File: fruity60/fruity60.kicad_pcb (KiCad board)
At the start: 2 copper layers, 126 parts

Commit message: Basic layout of switches
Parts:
- MX4A1: footprint MX_Only:MXOnly-1U -> MX_Only:MXOnly-1.5U
- moved MX0 382.1 mm to (-69.8, 65.1)
- moved D24 375.6 mm to (-26.4, 2.21)
- moved D3 375.6 mm to (-46.6, 26.4)
- moved D5 375.6 mm to (-20.6, 2.21)
- moved D11 375.6 mm to (-40.8, 19.7)
- moved D13 375.6 mm to (-46.6, 23.1)
- moved D27 375.6 mm to (-46.6, 19.7)
- moved D6 375.6 mm to (-26.4, 5.56)
- moved MX1 348.0 mm to (-50.8, 65.1)
- moved MX3 344.7 mm to (-12.7, 65.1)
- moved MX2 330.1 mm to (-31.8, 65.1)
- moved MX11 309.5 mm to (-41.3, 84.1)
- moved MX12 307.5 mm to (-22.2, 84.1)
- moved D19 303.2 mm to (154.6, 0.21)
- moved D32 303.2 mm to (148.9, 0.21)
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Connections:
- JP1 pad 1: /DFU -> (no net)
- JP1 pad 13: GND -> (no net)
- JP1 pad 14: /AREF -> (no net)
- JP1 pad 15: +3V3 -> (no net)
- JP1 pad 16: /RST -> (no net)
- JP1 pad 4: /MISO -> (no net)
- JP1 pad 5: /MOSI -> (no net)
- JP1 pad 6: /SCK -> (no net)
- JP2 pad 1: VBAT -> (no net)
- JP2 pad 2: /EN -> (no net)
- JP2 pad 3: VBUS -> (no net)

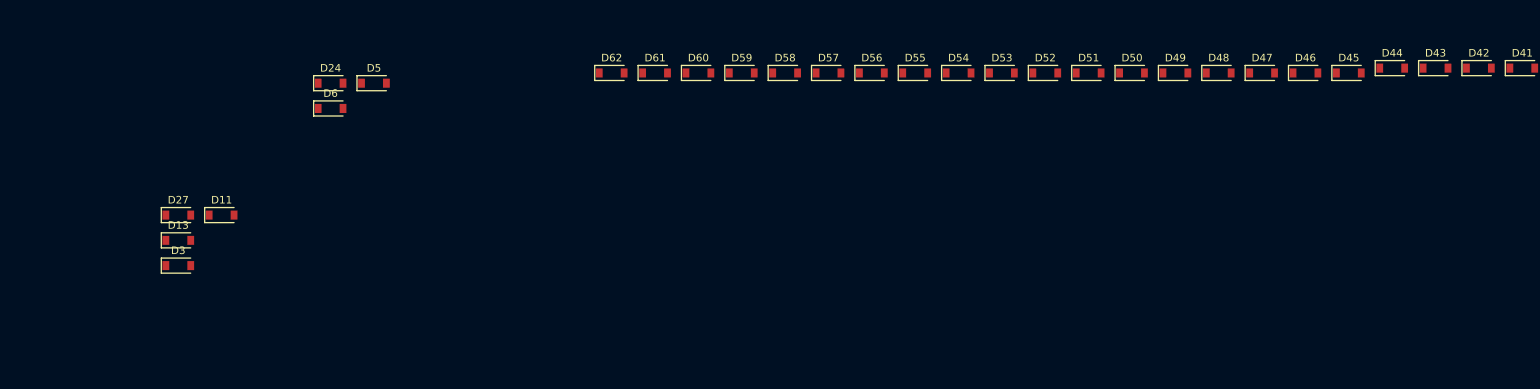
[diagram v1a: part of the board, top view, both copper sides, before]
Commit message: move some diodes around
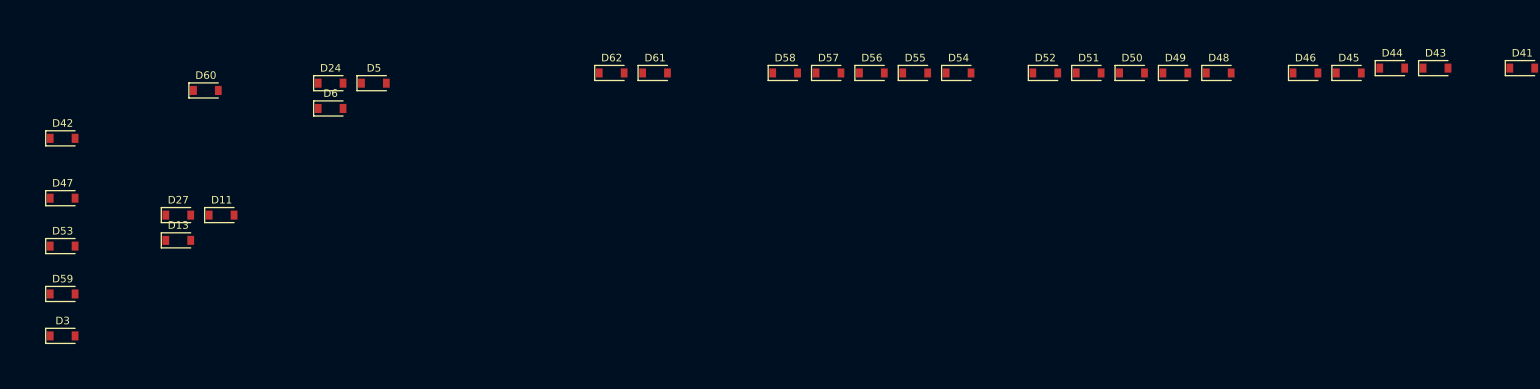
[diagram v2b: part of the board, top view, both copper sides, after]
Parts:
- moved D42 188.0 mm to (-61.9, 9.53)
- moved D47 159.9 mm to (-61.9, 17.5)
- moved D53 126.7 mm to (-61.9, 23.8)
- moved D59 94.7 mm to (-61.9, 30.2)
- moved D60 65.4 mm to (-42.9, 3.17)
- moved D3 17.9 mm to (-61.9, 35.7)
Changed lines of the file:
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@@
     (uvia_dia 0.3)
     (uvia_drill 0.1)
-    (add_net +3V3)
-    (add_net /AREF)
-    (add_net /DFU)
-    (add_net /EN)
-    (add_net /MISO)
-    (add_net /MOSI)
-    (add_net /RST)
-    (add_net /SCK)
     (add_net B5)
     (add_net B6)
@@
     (add_net F6)
     (add_net F7)
-    (add_net GND)
     (add_net "Net-(D1-Pad2)")
     (add_net "Net-(D10-Pad2)")
@@
     (add_net "Net-(D8-Pad2)")
     (add_net "Net-(D9-Pad2)")
-    (add_net VBAT)
-    (add_net VBUS)
   )
   (module MX_Only:MXOnly-1.5U (layer F.Cu)
@@
   )
   (module Diodes_SMD:D_SOD-123 (layer F.Cu)
-    (at 22.3925 0.855)
+    (at -42.925 3.175)
     (descr SOD-123)
     (tags SOD-123)
@@
   )
   (module Diodes_SMD:D_SOD-123 (layer F.Cu)
-    (at 28.1425 0.855)
+    (at -61.9125 30.1625)
     (descr SOD-123)
     (tags SOD-123)
@@
   )
   (module Diodes_SMD:D_SOD-123 (layer F.Cu)
-    (at 62.6425 0.855)
+    (at -61.9125 23.8125)
     (descr SOD-123)
     (tags SOD-123)
@@
   )
   (module Diodes_SMD:D_SOD-123 (layer F.Cu)
-    (at 97.1425 0.855)
+    (at -61.9125 17.4625)
     (descr SOD-123)
     (tags SOD-123)
@@
   )
   (module Diodes_SMD:D_SOD-123 (layer F.Cu)
-    (at 125.8925 0.215)
+    (at -61.9125 9.525)
     (descr SOD-123)
     (tags SOD-123)
@@
   )
   (module Diodes_SMD:D_SOD-123 (layer F.Cu)
-    (at -46.5825 26.4025)
+    (at -61.9125 35.71875)
     (descr SOD-123)
     (tags SOD-123)

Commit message: flip diodes. Thanks Skully
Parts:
- removed the D1 at (193.7, 23.8)
- removed the D27 at (-46.6, 19.7)
- added D0: D_Small, Diodes_SMD:D_SOD-123, B.Cu at (-70.6, 49.2)
- added D34: D_Small, Diodes_SMD:D_SOD-123, B.Cu at (10.3, 40.5)
- D1: renamed from D7; moved to B.Cu
- D10: renamed from D2; moved to B.Cu
- D11: renamed from D8; moved to B.Cu
- D12: renamed from D14; moved to B.Cu
- D13: renamed from D20; moved to B.Cu
- D14: renamed from D25; moved to B.Cu
- D15: renamed from D30; moved to B.Cu
- D16: renamed from D36; moved to B.Cu
- D17: renamed from D41; moved to B.Cu
- D18: renamed from D46; moved to B.Cu
- D19: renamed from D52; moved to B.Cu
- D1A1: renamed from D58; moved to B.Cu
- D2: renamed from D13; moved to B.Cu
- D20: renamed from D3; moved to B.Cu
- D21: renamed from D9; moved to B.Cu
- D22: renamed from D15; moved to B.Cu
- D23: renamed from D21; moved to B.Cu
- D24: renamed from D26; moved to B.Cu
- D25: renamed from D31; moved to B.Cu
- D26: renamed from D37; moved to B.Cu
- D27: renamed from D42; moved to B.Cu
- D28: renamed from D47; moved to B.Cu
- D29: renamed from D53; moved to B.Cu
- D2A1: renamed from D59; moved to B.Cu
- D3: renamed from D19; moved to B.Cu
- D30: renamed from D4; moved to B.Cu
- D31: renamed from D10; moved to B.Cu
- D32: renamed from D16; moved to B.Cu
- D33: renamed from D22; moved to B.Cu
- D35: renamed from D32; moved to B.Cu
- D36: renamed from D38; moved to B.Cu
- D37: renamed from D43; moved to B.Cu
- D38: renamed from D48; moved to B.Cu
- D39: renamed from D54; moved to B.Cu
- D3A1: renamed from D60; moved to B.Cu
- D4: renamed from D24; moved to B.Cu
- D40: renamed from D5; moved to B.Cu
- D41: renamed from D11; moved to B.Cu
- D42: renamed from D17; moved to B.Cu
- D45: renamed from D33; moved to B.Cu
- D48: renamed from D49; moved to B.Cu
- D49: renamed from D55; moved to B.Cu
- D4A1: renamed from D61; moved to B.Cu
- D5: renamed from D29; moved to B.Cu
- D50: renamed from D6; moved to B.Cu
- D51: renamed from D12; moved to B.Cu
- D52: renamed from D18; moved to B.Cu
- D53: renamed from D23; moved to B.Cu
- D54: renamed from D28; moved to B.Cu
- D55: renamed from D34; moved to B.Cu
- D56: renamed from D39; moved to B.Cu
- D57: renamed from D44; moved to B.Cu
- D58: renamed from D50; moved to B.Cu
- D59: renamed from D56; moved to B.Cu
- D5A1: renamed from D62; moved to B.Cu
- D6: renamed from D35; moved to B.Cu
- D7: renamed from D40; moved to B.Cu
- D8: renamed from D45; moved to B.Cu
- D9: renamed from D51; moved to B.Cu
- DA1: renamed from D57; moved to B.Cu
- moved D10 269.3 mm to (-68.3, 46.8), turned to 270 degrees
- moved D1 260.6 mm to (-52.4, 50.0), turned to 270 degrees
- moved D30 250.6 mm to (-63.5, 42.9), turned to 270 degrees
- moved D21 236.2 mm to (-47.6, 45.2), turned to 90 degrees
- moved D12 235.2 mm to (-33.3, 47.6), turned to 270 degrees
- moved D11 234.8 mm to (-50.0, 47.6), turned to 270 degrees
- moved D51 227.7 mm to (-40.5, 38.1), turned to 270 degrees
- moved D22 226.0 mm to (-31.0, 45.2), turned to 270 degrees
- moved D31 219.7 mm to (-45.2, 42.9), turned to 270 degrees
- moved D32 210.0 mm to (-28.6, 42.9), turned to 270 degrees
- moved D33 203.8 mm to (-8.73, 40.5), turned to 270 degrees
- moved D23 199.9 mm to (-11.1, 42.9), turned to 270 degrees
- moved D14 197.0 mm to (5.56, 45.2), turned to 270 degrees
- moved D52 192.0 mm to (-23.8, 38.1), turned to 270 degrees
- moved D42 190.3 mm to (-26.2, 40.5), turned to 270 degrees
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
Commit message: Align diodes better
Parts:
- moved D18 8.77 mm to (87.3, 48.4)
- moved D38 8.77 mm to (92.1, 43.7)
- moved D48 8.77 mm to (94.5, 41.3)
- moved D58 8.77 mm to (96.8, 38.9)
- moved D8 8.77 mm to (84.9, 50.8)
- moved D28 8.77 mm to (89.7, 46.0)
- moved D17 7.98 mm to (68.3, 46.0)
- moved D27 7.98 mm to (70.6, 43.7)
- moved D37 7.98 mm to (73.0, 41.3)
- moved D57 7.98 mm to (75.4, 38.9)
- moved D7 7.98 mm to (65.9, 48.4)
- moved D3A1 7.19 mm to (130.2, 43.7)
- moved D4A1 7.19 mm to (132.6, 41.3)
- moved D25 7.19 mm to (32.5, 46.0)
- moved D36 7.19 mm to (54.0, 41.3)
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
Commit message: Line up diodes for more pleasing look
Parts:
- D0, D1, D10, D11, D12, D13, D14, D15, D16, D17, D18, D19, D1A1, D2, D20, D21, D22, D23, D24, D25, D26, D27, D28, D29, D2A1, D3, D30, D31, D32, D33, D34, D35, D36, D37, D38, D39, D3A1, D4, D40, D41, D42, D45, D48, D49, D4A1, D5, D50, D51, D52, D53, D54, D55, D56, D57, D58, D59, D5A1, D6, D7, D8, D9, DA1: moved to F.Cu
- moved D50 198.0 mm to (142.1, 50.8)
- moved D51 181.4 mm to (144.5, 50.8)
- moved D52 164.7 mm to (146.8, 50.8)
- moved D53 150.5 mm to (149.2, 50.8)
- moved D54 133.9 mm to (151.6, 50.8)
- moved D55 114.9 mm to (154.0, 50.8)
- moved D56 99.9 mm to (155.6, 50.8)
- moved D57 83.4 mm to (158.0, 50.8)
- moved D58 64.6 mm to (160.3, 50.8)
- moved D59 48.3 mm to (162.7, 50.8)
- moved D5A1 32.4 mm to (165.1, 50.8)
- moved D13 2.38 mm to (-7.94, 48.4)
- moved D14 2.38 mm to (11.1, 48.4)
- moved D16 2.38 mm to (49.2, 48.4)
- moved D17 2.38 mm to (68.3, 48.4)
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
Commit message: Clean ups
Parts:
- moved D56 1.12 mm to (156.4, 50.0)
- moved D5A1 1.12 mm to (165.9, 50.0)
- moved D57 1.12 mm to (158.8, 50.0)
- moved D58 1.12 mm to (161.1, 50.0)
- moved D59 1.12 mm to (163.5, 50.0)
- moved D50 0.79 mm to (142.1, 50.0)
- moved D51 0.79 mm to (144.5, 50.0)
- moved D52 0.79 mm to (146.8, 50.0)
- moved D53 0.79 mm to (149.2, 50.0)
- moved D54 0.79 mm to (151.6, 50.0)
- moved D55 0.79 mm to (154.0, 50.0)

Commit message: Use 2.54 straight headers not angled
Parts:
- JP1: footprint Pin_Headers:Pin_Header_Angled_1x16_Pitch1.00mm -> Pin_Headers:Pin_Header_Straight_1x16_Pitch2.54mm
- JP2: footprint Pin_Headers:Pin_Header_Angled_1x12_Pitch1.00mm -> Pin_Headers:Pin_Header_Straight_1x12_Pitch2.54mm
- moved JP1 31.6 mm to (165.9, 39.7), turned to 90 degrees
- moved JP2 13.7 mm to (193.7, 50.8), turned to 270 degrees
- moved D50 7.98 mm to (134.1, 50.8)
- moved D51 7.98 mm to (136.5, 50.8)
- moved D52 7.98 mm to (138.9, 50.8)
- moved D53 7.98 mm to (141.3, 50.8)
- moved D54 7.98 mm to (143.7, 50.8)
- moved D55 7.98 mm to (146.1, 50.8)
- moved D56 7.98 mm to (148.4, 50.8)
- moved D57 7.98 mm to (150.8, 50.8)
- moved D58 7.98 mm to (153.2, 50.8)
- moved D59 7.98 mm to (155.6, 50.8)
- moved D5A1 7.98 mm to (158.0, 50.8)

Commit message: Routing weirdness
 May need to change footprint for diodes
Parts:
- moved D40 11.1 mm to (-57.9, 52.4)
- moved D41 11.1 mm to (-38.9, 52.4)
- moved D42 11.1 mm to (-19.8, 52.4)
- moved D48 11.1 mm to (94.5, 52.4)
- moved D49 11.1 mm to (113.5, 52.4)
- moved D4A1 11.1 mm to (132.6, 52.4)
- moved D45 10.3 mm to (37.3, 51.6)
- moved D30 7.14 mm to (-60.3, 50.8)
- moved D31 7.14 mm to (-41.3, 50.8)
- moved D32 7.14 mm to (-22.2, 50.8)
- moved D33 7.14 mm to (-3.17, 50.8)
- moved D34 7.14 mm to (15.9, 50.8)
- moved D35 7.14 mm to (34.9, 50.8)
- moved D36 7.14 mm to (54.0, 50.8)
- moved D37 7.14 mm to (73.0, 50.8)
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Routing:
- net F7: track 0.00 -> 366.3 mm
- net F6: track 0.00 -> 352.0 mm, vias 0 -> 2
- net F5: track 0.00 -> 338.8 mm
- net F4: track 0.00 -> 298.0 mm
- net F0: track 0.00 -> 283.4 mm
- net F1: track 0.00 -> 277.0 mm
- net B6: track 0.00 -> 249.4 mm
- net D7: track 0.00 -> 244.8 mm
- net B5: track 0.00 -> 243.0 mm
- net C6: track 0.00 -> 239.4 mm
- net C7: track 0.00 -> 239.1 mm
- net D2: track 0.00 -> 220.8 mm
- net B7: track 0.00 -> 214.8 mm
- net D3: track 0.00 -> 197.3 mm
- net D6: track 0.00 -> 146.1 mm
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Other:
- net class Power added: clearance 0.2, trace_width 0.381, via_dia 0.8, via_drill 0.4
